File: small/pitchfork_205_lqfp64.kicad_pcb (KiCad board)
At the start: 2 copper layers, 68.3 x 32.9 mm, 100 parts, among them IC1 STM32F2XX_64LQFP, U1 LM3670, U3 MCP73832-2, U4 NRF24L01+, U6 MICROSDCARD, U8 TSV912, U9 TC75W57, X1 25MHz, X2 16MHz, Y1 CHIP_ANTENNA

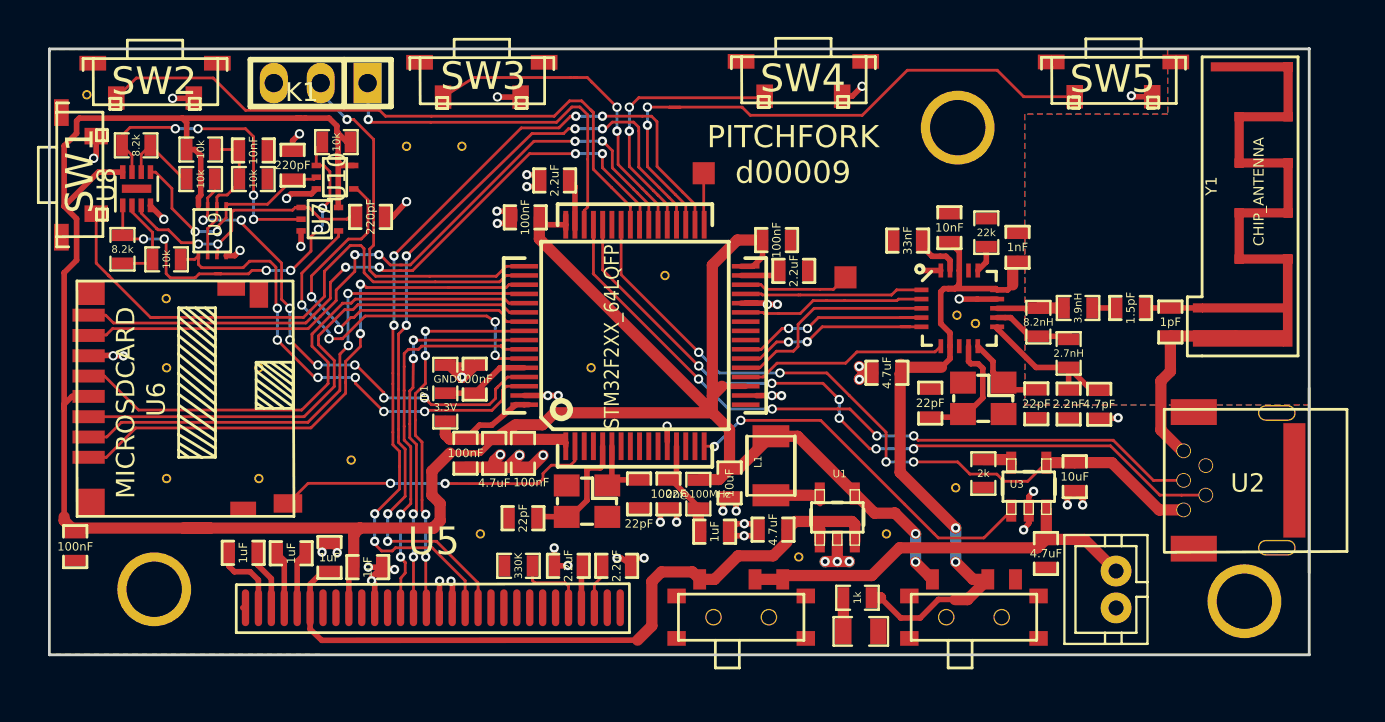
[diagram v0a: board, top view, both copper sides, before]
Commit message: [fix] bugs from 2nd revision fixed
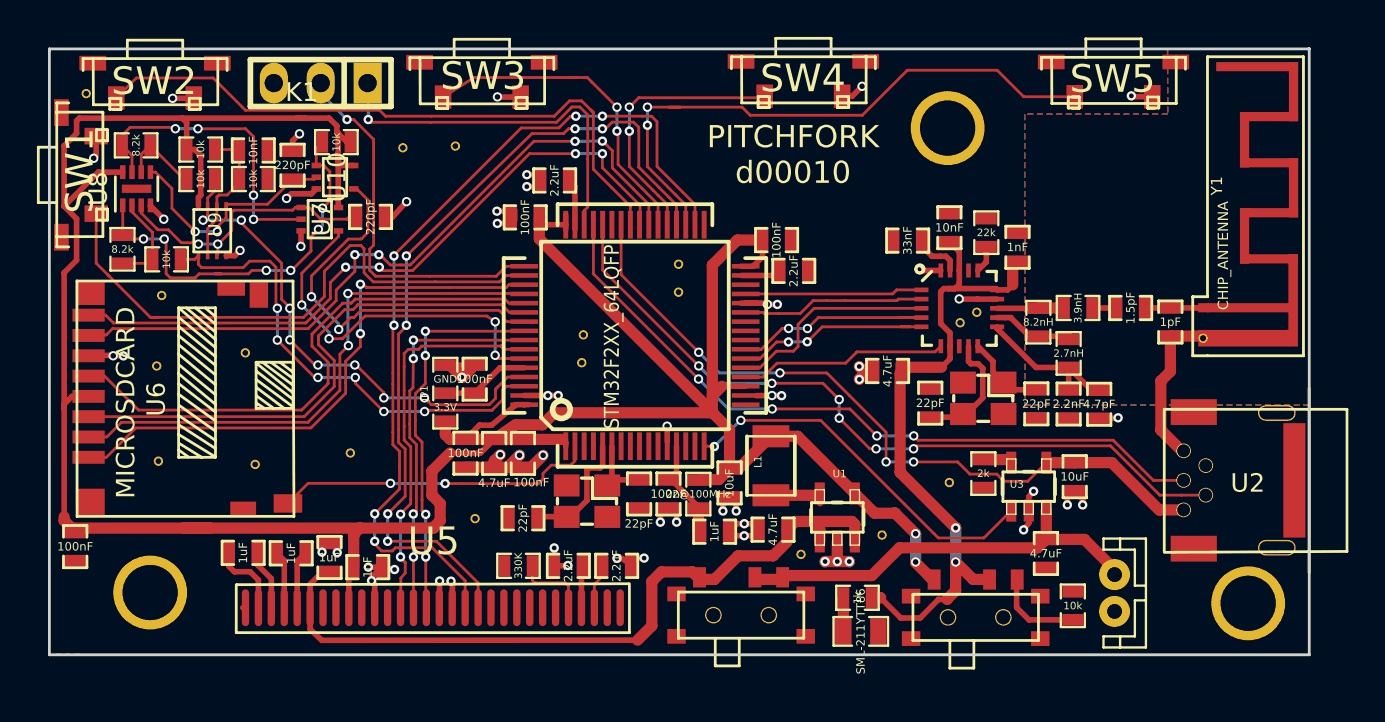
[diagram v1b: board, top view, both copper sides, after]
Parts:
- removed the 1Pin_12mil_VIA at (215.8, 110.2)
- removed the 1Pin_12mil_VIA at (189.0, 101.0)
- removed the 1Pin_12mil_VIA at (196.0, 113.0)
- removed the 1Pin_12mil_VIA at (200.0, 108.0)
- removed the 1Pin_12mil_VIA at (173.0, 113.0)
- removed the 1Pin_12mil_VIA at (173.0, 119.0)
- removed the 1Pin_12mil_VIA at (178.0, 113.0)
- removed the 1Pin_12mil_VIA at (183.0, 118.0)
- removed the 1Pin_12mil_VIA at (178.0, 119.0)
- removed the 1Pin_12mil_VIA at (190.0, 122.0)
- removed the 1Pin_12mil_VIA at (216.8, 110.6)
- removed the 1Pin_12mil_VIA at (168.7, 98.2)
- removed the 1Pin_12mil_VIA at (173.0, 109.2)
- removed the 1Pin_12mil_VIA at (188.3, 112.0)
- removed the 1Pin_12mil_VIA at (215.8, 119.5)
- removed the 1Pin_12mil_VIA at (212.0, 122.0)
- removed the 1Pin_12mil_VIA at (207.2, 123.2)
- removed the 1Pin_12mil_VIA at (186.0, 101.0)
- removed the 1Pin_15mil_VIA at (215.9, 100.0)
- removed the 1Pin_15mil_VIA at (172.3, 125.0)
- removed the 1Pin_15mil_VIA at (231.4, 125.6)
- removed the ? at (204.1, 126.5)
- removed the ? at (216.7, 126.5)
- removed the ? at (209.8, 108.1)
- removed the ? at (202.1, 102.4)
- removed SM0603_Opendous: 4.7uF, opendous:SM0603_Opendous
- added 1Pin_12mil_VIA: VAL**, opendous:1Pin_12mil_VIA, F.Cu at (185.8, 101.1)
- added 1Pin_12mil_VIA: VAL**, opendous:1Pin_12mil_VIA, F.Cu at (195.5, 112.7)
- added 1Pin_12mil_VIA: VAL**, opendous:1Pin_12mil_VIA, F.Cu at (200.7, 107.4)
- added 1Pin_12mil_VIA: VAL**, opendous:1Pin_12mil_VIA, F.Cu at (211.8, 122.1)
- added 1Pin_12mil_VIA: VAL**, opendous:1Pin_12mil_VIA, F.Cu at (215.4, 119.2)
- added 1Pin_12mil_VIA: VAL**, opendous:1Pin_12mil_VIA, F.Cu at (200.7, 108.9)
- added 1Pin_12mil_VIA: VAL**, opendous:1Pin_12mil_VIA, F.Cu at (195.6, 111.2)
- added 1Pin_12mil_VIA: VAL**, opendous:1Pin_12mil_VIA, F.Cu at (216.9, 110.0)
- added 1Pin_12mil_VIA: VAL**, opendous:1Pin_12mil_VIA, F.Cu at (216.0, 110.6)
- added 1Pin_12mil_VIA: VAL**, opendous:1Pin_12mil_VIA, F.Cu at (207.4, 123.1)
- added 1Pin_12mil_VIA: VAL**, opendous:1Pin_12mil_VIA, F.Cu at (168.6, 98.1)
- added 1Pin_12mil_VIA: VAL**, opendous:1Pin_12mil_VIA, F.Cu at (188.6, 101.0)
- added 1Pin_12mil_VIA: VAL**, opendous:1Pin_12mil_VIA, F.Cu at (172.7, 109.1)
- added 1Pin_12mil_VIA: VAL**, opendous:1Pin_12mil_VIA, F.Cu at (172.5, 112.9)
- added 1Pin_12mil_VIA: VAL**, opendous:1Pin_12mil_VIA, F.Cu at (172.6, 118.1)
- added 1Pin_12mil_VIA: VAL**, opendous:1Pin_12mil_VIA, F.Cu at (177.3, 112.2)
- added 1Pin_12mil_VIA: VAL**, opendous:1Pin_12mil_VIA, F.Cu at (177.8, 118.2)
- added 1Pin_12mil_VIA: VAL**, opendous:1Pin_12mil_VIA, F.Cu at (183.0, 117.6)
- added 1Pin_12mil_VIA: VAL**, opendous:1Pin_12mil_VIA, F.Cu at (189.7, 121.2)
- added 1Pin_15mil_VIA: VAL**, opendous:1Pin_15mil_VIA, F.Cu at (172.1, 125.2)
- added 1Pin_15mil_VIA: VAL**, opendous:1Pin_15mil_VIA, F.Cu at (215.3, 100.0)
- added 1Pin_15mil_VIA: VAL**, opendous:1Pin_15mil_VIA, F.Cu at (231.6, 125.8)
- added ?: , pitchforkbuttons:EG1257, F.Cu at (204.1, 126.4)
- added ?: , pitchforkbuttons:EG1257, F.Cu at (216.8, 126.5)
- added C36: 4.7uF, opendous:SM0603_Opendous, F.Cu at (212.1, 113.2)
- added R12: 10k, opendous:0603_Opendous, F.Cu at (222.1, 125.9)
- D1: value (none) -> SML-211YTT86
- U8: value TSV912 -> (none); footprint DFN-8-1EP_2x2mm_Pitch0.5mm -> pitchforkv02:DFN-8-1EP_2x2mm_Pitch0.5mm
- U9: value TC75W57 -> (none)
- Y1: footprint Antenna_Meander_2.4GHz_TI_AN043 -> opendous:Antenna_Meander_2.4GHz_TI_AN043
- moved Y1 9.34 mm to (229.4, 108.5)
- moved ? 0.21 mm to (224.4, 125.2)
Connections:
- IC1 pad 30: /spare2 -> Net-(IC1-Pad30)
- IC1 pad 33: /spare3 -> Net-(IC1-Pad33)
- U6 pad 10: Net-(U6-Pad10) -> GND
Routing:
- net Net-(C16-Pad1): track 39.1 -> 25.5 mm, vias 2 -> 0
- net /vdd: track 171.0 -> 184.0 mm, vias 2 -> 4
- net /spare2: track 6.03 -> 0.00 mm
- net Net-(R12-Pad2): track 0.00 -> 4.84 mm
- net /spare3: track 3.06 -> 0.00 mm
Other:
- board text added: "PITCHFORK d00010"
- board text removed: "PITCHFORK d00009"
